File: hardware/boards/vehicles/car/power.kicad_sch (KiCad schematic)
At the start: 19 parts, among them J8 Conn_01x04_Socket, U4 TPS54302, U5 AMS1117-3.3

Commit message: car PCB
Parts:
- removed J8: Conn_01x04_Socket, Connector_PinHeader_2.54mm:PinHeader_1x04_P2.54mm_Vertical, symbol Connector:Conn_01x04_Socket
- C15: renamed from C41; footprint Capacitor_THT:CP_Radial_D5.0mm_P2.00mm -> common:CP_Elec_6.3x5.4
- C17: renamed from C43; footprint Capacitor_THT:CP_Radial_D5.0mm_P2.00mm -> common:CP_Elec_6.3x5.4
- C9: renamed from C19; footprint Capacitor_THT:CP_Radial_D5.0mm_P2.00mm -> Capacitor_SMD:CP_Elec_4x5.4
- D4: renamed from D12; value 1N400x -> RS1MFA; footprint Diode_THT:D_DO-41_SOD81_P2.54mm_Vertical_AnodeUp -> common:D_SOD123
- L1: footprint Connector_PinHeader_2.54mm:PinHeader_1x02_P2.54mm_Vertical -> common:Inductor_octogone
- renumbered C20 to C10, C21 to C11, C22 to C12, C23 to C13, C24 to C14, C42 to C16, R29 to R10, R30 to R11, R31 to R12, R23 to R8, R25 to R9, U4 to U2, U5 to U3
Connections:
- net 12V renamed VIN
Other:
- note removed: "3V3 @ 1A"
- note removed: "5V @ 3A"
- note removed: "L1 needs a saturation current of at least 4A"
- note removed: "This will get hot. We'll have to add a heatsink"
- note removed: "We'll need a large copper pour (Power Ground) on both the top and bottom layers of the pcb for heat dissipation"

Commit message: added interactive bom for lidar and car
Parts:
- D4: value RS1MFA -> 1N4007
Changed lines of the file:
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@@
 			)
 		)
-		(property "Value" "RS1MFA"
+		(property "Value" "1N4007"
 			(at 201.93 83.82 0)
 			(effects

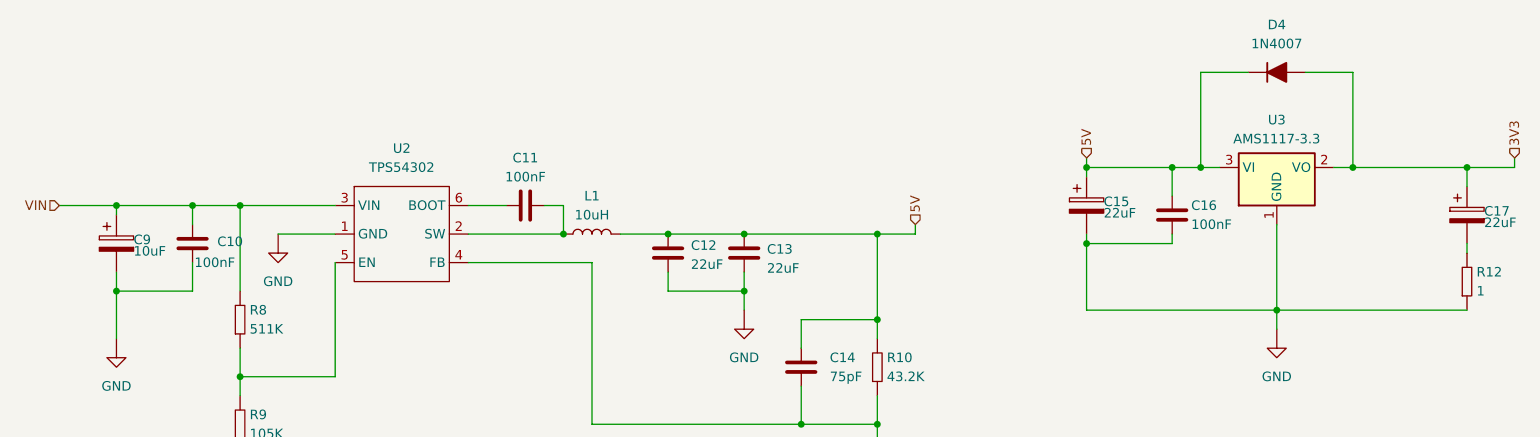
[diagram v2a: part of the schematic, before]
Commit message: change kicad default to custom
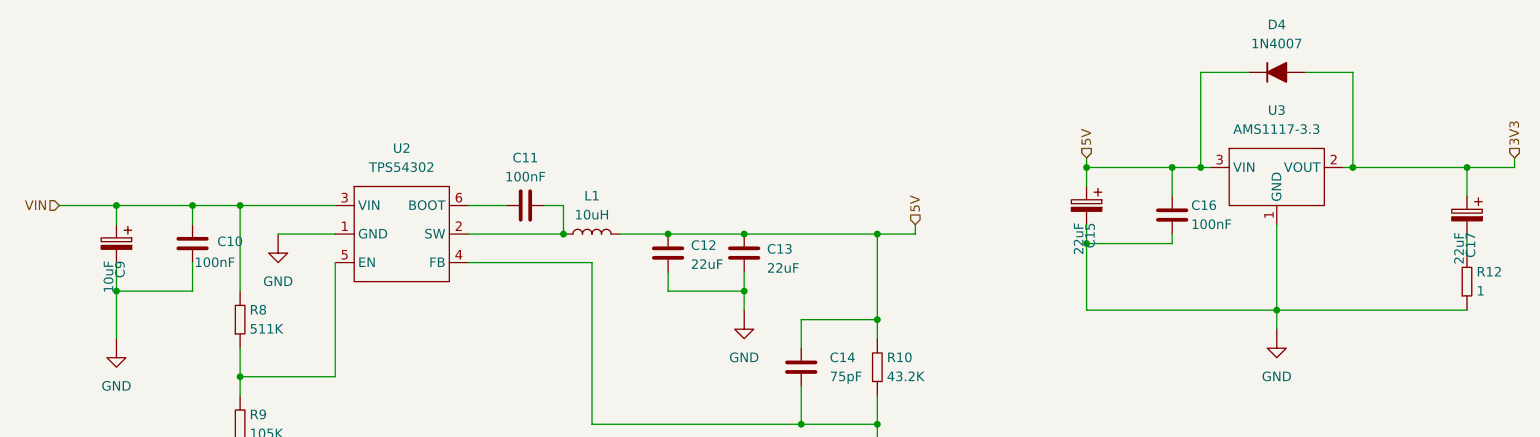
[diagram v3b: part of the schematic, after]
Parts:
- C10, C11, C12, C13, C14, C16: footprint Capacitor_SMD:C_0603_1608Metric_Pad1.08x0.95mm_HandSolder -> common:C_0603
- C15, C17: symbol Device:C_Polarized -> common:Capacitor_Electrolytic
- C9: footprint Capacitor_SMD:CP_Elec_4x5.4 -> common:CP_Elec_4x5.4; symbol Device:C_Polarized -> common:Capacitor_Electrolytic
- R10, R11, R12, R8, R9: footprint Resistor_SMD:R_0603_1608Metric_Pad0.98x0.95mm_HandSolder -> common:R_0603
- U2: footprint Package_TO_SOT_SMD:TSOT-23-6_HandSoldering -> regulator:TPS54302_TSOT-23
- U3: footprint Package_TO_SOT_SMD:SOT-223-3_TabPin2 -> regulator:AMS1117-SOT223; symbol Regulator_Linear:AMS1117-3.3 -> regulator:AMS1117
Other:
- moved on the sheet: C15, C17, C9
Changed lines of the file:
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@@
 	(paper "A4")
+	(junction
+		(at 106.68 109.22)
+		(diameter 0)
+		(color 0 0 0 0)
+	)
+	(junction
+		(at 57.15 105.41)
+		(diameter 0)
+		(color 0 0 0 0)
+	)
+	(junction
+		(at 148.59 134.62)
+		(diameter 0)
+		(color 0 0 0 0)
+	)
+	(junction
+		(at 201.93 119.38)
+		(diameter 0)
+		(color 0 0 0 0)
+	)
 	(junction
 		(at 191.77 100.33)
@@
 	)
 	(junction
-		(at 106.68 109.22)
-		(diameter 0)
-		(color 0 0 0 0)
-	)
-	(junction
-		(at 57.15 105.41)
-		(diameter 0)
-		(color 0 0 0 0)
-	)
-	(junction
-		(at 148.59 134.62)
-		(diameter 0)
-		(color 0 0 0 0)
-	)
-	(junction
-		(at 201.93 119.38)
-		(diameter 0)
-		(color 0 0 0 0)
-	)
-	(junction
 		(at 46.99 105.41)
 		(diameter 0)
@@
 	)
 	(junction
-		(at 212.09 100.33)
-		(diameter 0)
-		(color 0 0 0 0)
-	)
-	(junction
 		(at 63.5 105.41)
 		(diameter 0)
@@
 	)
 	(junction
+		(at 212.09 100.33)
+		(diameter 0)
+		(color 0 0 0 0)
+	)
+	(junction
 		(at 130.81 116.84)
 		(diameter 0)
@@
 	(wire
 		(pts
-			(xy 176.53 100.33) (xy 176.53 101.6)
+			(xy 176.53 100.33) (xy 176.53 102.87)
 		)
 		(stroke
@@
 	(wire
 		(pts
-			(xy 191.77 100.33) (xy 194.31 100.33)
-		)
-		(stroke
-			(width 0)
-			(type default)
-		)
-	)
-	(wire
-		(pts
 			(xy 138.43 134.62) (xy 148.59 134.62)
 		)
@@
 	(wire
 		(pts
-			(xy 209.55 100.33) (xy 212.09 100.33)
+			(xy 46.99 105.41) (xy 46.99 107.95)
 		)
 		(stroke
@@
 	(wire
 		(pts
-			(xy 46.99 114.3) (xy 46.99 116.84)
+			(xy 46.99 113.03) (xy 46.99 116.84)
 		)
 		(stroke
@@
 	(wire
 		(pts
+			(xy 210.82 100.33) (xy 212.09 100.33)
+		)
+		(stroke
+			(width 0)
+			(type default)
+		)
+	)
+	(wire
+		(pts
 			(xy 63.5 105.41) (xy 63.5 116.84)
 		)
@@
 	(wire
 		(pts
-			(xy 227.33 110.49) (xy 227.33 111.76)
-		)
-		(stroke
-			(width 0)
-			(type default)
-		)
-	)
-	(wire
-		(pts
 			(xy 176.53 100.33) (xy 187.96 100.33)
 		)
@@
 	(wire
 		(pts
-			(xy 176.53 109.22) (xy 176.53 110.49)
+			(xy 176.53 107.95) (xy 176.53 110.49)
 		)
 		(stroke
@@
 	(wire
 		(pts
-			(xy 46.99 105.41) (xy 46.99 106.68)
-		)
-		(stroke
-			(width 0)
-			(type default)
-		)
-	)
-	(wire
-		(pts
 			(xy 212.09 100.33) (xy 227.33 100.33)
 		)
@@
 	(wire
 		(pts
+			(xy 191.77 100.33) (xy 193.04 100.33)
+		)
+		(stroke
+			(width 0)
+			(type default)
+		)
+	)
+	(wire
+		(pts
+			(xy 227.33 109.22) (xy 227.33 111.76)
+		)
+		(stroke
+			(width 0)
+			(type default)
+		)
+	)
+	(wire
+		(pts
 			(xy 176.53 110.49) (xy 187.96 110.49)
 		)
@@
 	(wire
 		(pts
-			(xy 227.33 100.33) (xy 227.33 102.87)
+			(xy 227.33 100.33) (xy 227.33 104.14)
 		)
 		(stroke
@@
 			)
 		)
-		(property "Footprint" "Resistor_SMD:R_0603_1608Metric_Pad0.98x0.95mm_HandSolder"
+		(property "Footprint" "common:R_0603"
 			(at 148.59 127 0)
 			(effects
@@
 			)
 		)
-		(property "Footprint" "Resistor_SMD:R_0603_1608Metric_Pad0.98x0.95mm_HandSolder"
+		(property "Footprint" "common:R_0603"
 			(at 63.5 120.65 0)
 			(effects
@@
 	)
 	(symbol
-		(lib_id "Device:C_Polarized")
-		(at 46.99 110.49 0)
+		(lib_id "common:Capacitor_Electrolytic")
+		(at 46.99 110.49 270)
 		(unit 1)
 		(exclude_from_sim no)
@@
 		(dnp no)
 		(property "Reference" "C9"
-			(at 49.276 109.982 0)
+			(at 47.498 112.776 0)
 			(effects
 				(font
@@
 		)
 		(property "Value" "10uF"
-			(at 49.276 111.506 0)
+			(at 45.974 112.776 0)
 			(effects
 				(font
@@
 			)
 		)
-		(property "Footprint" "Capacitor_SMD:CP_Elec_4x5.4"
-			(at 47.9552 114.3 0)
+		(property "Footprint" "common:CP_Elec_4x5.4"
+			(at 46.99 110.49 0)
 			(effects
 				(font
@@
 			)
 		)
-		(property "Description" "Polarized capacitor"
-			(at 46.99 110.49 0)
+		(property "Description" "Electrolytic Capacitor"
+			(at 41.99 110.49 0)
 			(effects
 				(font
@@
 	)
 	(symbol
-		(lib_id "Device:C_Polarized")
-		(at 176.53 105.41 0)
+		(lib_id "common:Capacitor_Electrolytic")
+		(at 176.53 105.41 270)
 		(unit 1)
 		(exclude_from_sim no)
@@
 		(dnp no)
 		(property "Reference" "C15"
-			(at 178.816 104.902 0)
+			(at 177.038 107.696 0)
 			(effects
 				(font
@@
 		)
 		(property "Value" "22uF"
-			(at 178.816 106.426 0)
+			(at 175.514 107.696 0)
 			(effects
 				(font
@@
 		)
 		(property "Footprint" "common:CP_Elec_6.3x5.4"
-			(at 177.4952 109.22 0)
+			(at 176.53 105.41 0)
 			(effects
 				(font
@@
 			)
 		)
-		(property "Description" "Polarized capacitor"
-			(at 176.53 105.41 0)
+		(property "Description" "Electrolytic Capacitor"
+			(at 171.53 105.41 0)
 			(effects
 				(font
@@
 			)
 		)
-		(property "Footprint" "Capacitor_SMD:C_0603_1608Metric_Pad1.08x0.95mm_HandSolder"
+		(property "Footprint" "common:C_0603"
 			(at 130.81 111.76 0)
 			(effects
@@
 			)
 		)
-		(property "Footprint" "Package_TO_SOT_SMD:TSOT-23-6_HandSoldering"
+		(property "Footprint" "regulator:TPS54302_TSOT-23"
 			(at 85.09 118.11 0)
 			(effects
@@
 			)
 		)
-		(property "Footprint" "Resistor_SMD:R_0603_1608Metric_Pad0.98x0.95mm_HandSolder"
+		(property "Footprint" "common:R_0603"
 			(at 148.59 140.97 0)
 			(effects
@@
 			)
 		)
-		(property "Footprint" "Capacitor_SMD:C_0603_1608Metric_Pad1.08x0.95mm_HandSolder"
+		(property "Footprint" "common:C_0603"
 			(at 57.15 110.49 0)
 			(effects
@@
 			)
 		)
-		(property "Footprint" "Capacitor_SMD:C_0603_1608Metric_Pad1.08x0.95mm_HandSolder"
+		(property "Footprint" "common:C_0603"
 			(at 138.43 127 0)
 			(effects
@@
 	)
 	(symbol
-		(lib_id "Regulator_Linear:AMS1117-3.3")
+		(lib_id "regulator:AMS1117")
 		(at 201.93 100.33 0)
 		(unit 1)
@@
 		(fields_autoplaced yes)
 		(property "Reference" "U3"
-			(at 201.93 93.98 0)
+			(at 201.93 92.71 0)
 			(effects
 				(font
@@
 		)
 		(property "Value" "AMS1117-3.3"
-			(at 201.93 96.52 0)
-			(effects
-				(font
-					(size 1.27 1.27)
-				)
-			)
-		)
-		(property "Footprint" "Package_TO_SOT_SMD:SOT-223-3_TabPin2"
 			(at 201.93 95.25 0)
 			(effects
@@
 					(size 1.27 1.27)
 				)
+			)
+		)
+		(property "Footprint" "regulator:AMS1117-SOT223"
+			(at 201.93 100.33 0)
+			(effects
+				(font
+					(size 1.27 1.27)
+				)
 				(hide yes)
 			)
 		)
 		(property "Datasheet" "http://www.advanced-monolithic.com/pdf/ds1117.pdf"
-			(at 204.47 106.68 0)
-			(effects
-				(font
-					(size 1.27 1.27)
-				)
-				(hide yes)
-			)
-		)
-		(property "Description" "1A Low Dropout regulator, positive, 3.3V fixed output, SOT-223"
-			(at 201.93 100.33 0)
+			(at 201.93 121.33 0)
+			(effects
+				(font
+					(size 1.27 1.27)
+				)
+				(hide yes)
+			)
+		)
+		(property "Description" "Low Dropout (LDO) Voltage Regulator"
+			(at 201.93 118.83 0)
 			(effects
 				(font
@@
 		)
 		(pin "3"
+		)
+		(pin "4"
 		)
 		(instances
@@
 			)
 		)
-		(property "Footprint" "Capacitor_SMD:C_0603_1608Metric_Pad1.08x0.95mm_HandSolder"
+		(property "Footprint" "common:C_0603"
 			(at 101.6 105.41 0)
 			(effects
@@
 			)
 		)
-		(property "Footprint" "Resistor_SMD:R_0603_1608Metric_Pad0.98x0.95mm_HandSolder"
+		(property "Footprint" "common:R_0603"
 			(at 63.5 134.62 0)
 			(effects
@@
 			)
 		)
-		(property "Footprint" "Resistor_SMD:R_0603_1608Metric_Pad0.98x0.95mm_HandSolder"
+		(property "Footprint" "common:R_0603"
 			(at 227.33 115.57 0)
 			(effects
@@
 			)
 		)
-		(property "Footprint" "Capacitor_SMD:C_0603_1608Metric_Pad1.08x0.95mm_HandSolder"
+		(property "Footprint" "common:C_0603"
 			(at 187.96 106.68 0)
 			(effects
@@
 			)
 		)
-		(property "Footprint" "Capacitor_SMD:C_0603_1608Metric_Pad1.08x0.95mm_HandSolder"
+		(property "Footprint" "common:C_0603"
 			(at 120.65 111.76 0)
 			(effects
@@
 	)
 	(symbol
-		(lib_id "Device:C_Polarized")
-		(at 227.33 106.68 0)
+		(lib_id "common:Capacitor_Electrolytic")
+		(at 227.33 106.68 270)
 		(unit 1)
 		(exclude_from_sim no)
@@
 		(dnp no)
 		(property "Reference" "C17"
-			(at 229.616 106.172 0)
+			(at 227.838 108.966 0)
 			(effects
 				(font
@@
 		)
 		(property "Value" "22uF"
-			(at 229.616 107.696 0)
+			(at 226.314 108.966 0)
 			(effects
 				(font
@@
 		)
 		(property "Footprint" "common:CP_Elec_6.3x5.4"
-			(at 228.2952 110.49 0)
+			(at 227.33 106.68 0)
 			(effects
 				(font
@@
 			)
 		)
-		(property "Description" "Polarized capacitor"
-			(at 227.33 106.68 0)
-			(effects
-				(font
+		(property "Description" "Electrolytic Capacitor"
+			(at 222.33 106.68 0)
+			(effects
+				(font
